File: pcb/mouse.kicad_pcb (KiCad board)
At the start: 2 copper layers, 70 x 45 mm, 74 parts, among them J1 USB_C_Receptacle_USB2.0, J2 Conn_01x05, J3 Conn_02x03_Counter_Clockwise, J4 Conn_01x06, J5 Conn_01x06, SW1 SW_Push_SPDT, SW2 SW_Push_SPDT, SW3 SW_Push_SPDT, SW4 SW_Push_SPDT, SW5 RotaryEncoder, SW6 SW_Push, U1 pmw3360-t2qu, U2 TLV70018_SOT23-5, U3 STM32F042K6Tx, U4 TLV70033_SOT23-5

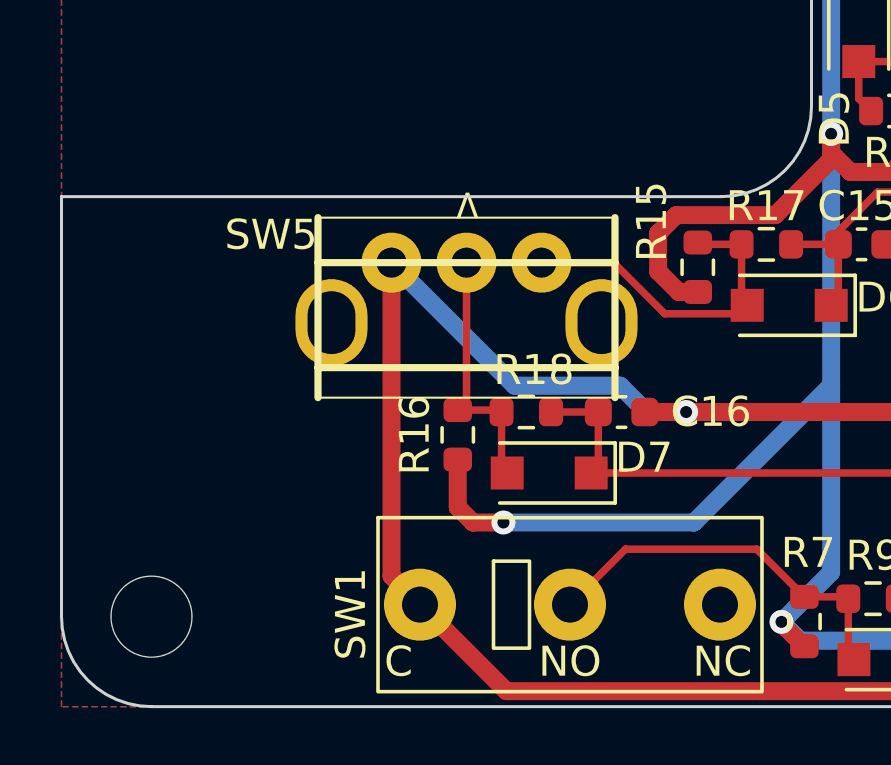
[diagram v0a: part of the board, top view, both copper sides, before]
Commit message: adjusted encoder position
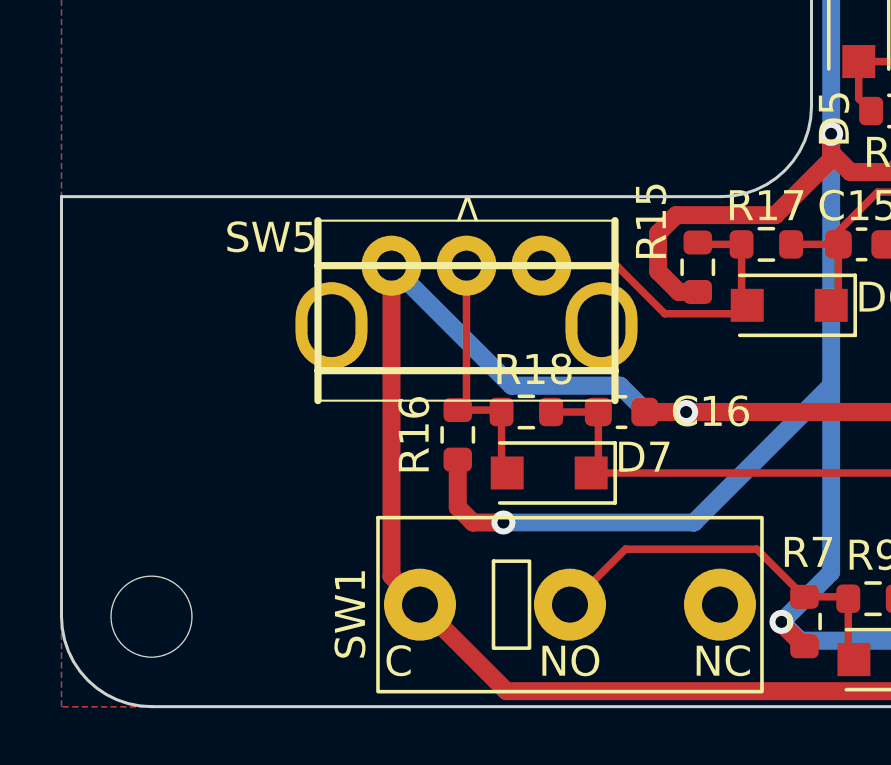
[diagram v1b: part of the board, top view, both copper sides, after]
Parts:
- moved SW5 0.10 mm to (113.5, 110.3)
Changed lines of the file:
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@@
   )
   (footprint "mouse:mouse_encoder" (layer "F.Cu")
-    (at 113.5 110.2 180)
+    (at 113.5 110.3 180)
     (property "Sheetfile" "buttons.kicad_sch")
     (property "Sheetname" "buttons")
@@
   (segment (start 111 120.65) (end 111.95 121.6) (width 0.6) (layer "F.Cu") (net 2))
   (segment (start 129.922 94.478) (end 130.82 94.478) (width 0.6) (layer "F.Cu") (net 2))
+  (segment (start 111 120.65) (end 111 110.3) (width 0.6) (layer "F.Cu") (net 2))
   (segment (start 107.005 93.915) (end 107.57 93.35) (width 0.6) (layer "F.Cu") (net 2))
   (segment (start 103.175 81.969) (end 103.769 81.969) (width 0.6) (layer "F.Cu") (net 2))
@@
   (segment (start 160.123 115.546) (end 161.10625 116.52925) (width 0.6) (layer "F.Cu") (net 2))
   (segment (start 140.214 95.113) (end 139.9186 95.113) (width 0.6) (layer "F.Cu") (net 2))
-  (segment (start 111 120.65) (end 111 110.2) (width 0.6) (layer "F.Cu") (net 2))
   (segment (start 129.8956 109.5502) (end 127.4858 109.5502) (width 0.6) (layer "F.Cu") (net 2))
   (via (at 123.571 91.821) (size 0.8) (drill 0.4) (layers "F.Cu" "B.Cu") (net 2))
@@
   (segment (start 138.14202 89.29782) (end 136.652 87.8078) (width 0.6) (layer "B.Cu") (net 2))
   (segment (start 123.571 91.821) (end 124.2568 91.821) (width 0.6) (layer "B.Cu") (net 2))
-  (segment (start 115.1 114.3) (end 111 110.2) (width 0.6) (layer "B.Cu") (net 2))
+  (segment (start 119.497 115.179) (end 118.618 114.3) (width 0.6) (layer "B.Cu") (net 2))
   (segment (start 110.0828 82.6) (end 110.8828 83.4) (width 0.6) (layer "B.Cu") (net 2))
   (segment (start 152.0124 86.5124) (end 147.7 82.2) (width 0.6) (layer "B.Cu") (net 2))
+  (segment (start 118.618 114.3) (end 115 114.3) (width 0.6) (layer "B.Cu") (net 2))
   (segment (start 138.14202 91.584193) (end 138.14202 89.29782) (width 0.6) (layer "B.Cu") (net 2))
   (segment (start 131.0984 115.452) (end 131.0984 119.77) (width 0.6) (layer "B.Cu") (net 2))
@@
   (segment (start 102.825 85.68) (end 102.825 94.32) (width 0.6) (layer "B.Cu") (net 2))
   (segment (start 102.825 85.68) (end 102.835034 85.690034) (width 0.6) (layer "B.Cu") (net 2))
+  (segment (start 115 114.3) (end 111 110.3) (width 0.6) (layer "B.Cu") (net 2))
   (segment (start 102.825 85.68) (end 102.9912 85.68) (width 0.6) (layer "B.Cu") (net 2))
-  (segment (start 119.497 115.179) (end 118.618 114.3) (width 0.6) (layer "B.Cu") (net 2))
   (segment (start 123.55 91.8) (end 112.15 91.8) (width 0.6) (layer "B.Cu") (net 2))
+  (segment (start 120.821 115.179) (end 119.497 115.179) (width 0.6) (layer "B.Cu") (net 2))
   (segment (start 152.7302 91.059) (end 152.2212 91.568) (width 0.6) (layer "B.Cu") (net 2))
   (segment (start 127.127 88.9508) (end 130.7084 88.9508) (width 0.6) (layer "B.Cu") (net 2))
@@
   (segment (start 155.2702 117.6528) (end 142.2654 117.6528) (width 0.6) (layer "B.Cu") (net 2))
   (segment (start 133.2992 117.6528) (end 142.2654 117.6528) (width 0.6) (layer "B.Cu") (net 2))
-  (segment (start 120.821 115.179) (end 119.497 115.179) (width 0.6) (layer "B.Cu") (net 2))
   (segment (start 140.4112 99.06) (end 140.3858 99.0346) (width 0.6) (layer "B.Cu") (net 2))
   (segment (start 154.7622 93.1926) (end 156.0796 93.1926) (width 0.6) (layer "B.Cu") (net 2))
@@
   (segment (start 104.4 82.6) (end 110.0828 82.6) (width 0.6) (layer "B.Cu") (net 2))
   (segment (start 124.2568 91.821) (end 127.127 88.9508) (width 0.6) (layer "B.Cu") (net 2))
-  (segment (start 118.618 114.3) (end 115.1 114.3) (width 0.6) (layer "B.Cu") (net 2))
   (segment (start 102.825 94.32) (end 107.005 94.32) (width 0.6) (layer "B.Cu") (net 2))
   (segment (start 132.7658 117.1194) (end 133.2992 117.6528) (width 0.6) (layer "B.Cu") (net 2))
@@
   (segment (start 122.67 111.436) (end 122.857 111.623) (width 0.25) (layer "F.Cu") (net 19))
   (segment (start 121.272 109.591) (end 121.209 109.528) (width 0.25) (layer "F.Cu") (net 19))
-  (segment (start 118.406676 110.2) (end 116 110.2) (width 0.25) (layer "F.Cu") (net 19))
+  (segment (start 120.109676 111.903) (end 118.506676 110.3) (width 0.25) (layer "F.Cu") (net 19))
+  (segment (start 118.506676 110.3) (end 116 110.3) (width 0.25) (layer "F.Cu") (net 19))
   (segment (start 122.67 109.591) (end 121.272 109.591) (width 0.25) (layer "F.Cu") (net 19))
-  (segment (start 120.109676 111.903) (end 118.406676 110.2) (width 0.25) (layer "F.Cu") (net 19))
   (segment (start 122.67 109.591) (end 122.67 111.436) (width 0.25) (layer "F.Cu") (net 19))
   (segment (start 122.857 111.623) (end 122.577 111.903) (width 0.25) (layer "F.Cu") (net 19))
+  (segment (start 113.208 115.116) (end 113.5 114.824) (width 0.25) (layer "F.Cu") (net 20))
   (segment (start 113.208 115.116) (end 114.606 115.116) (width 0.25) (layer "F.Cu") (net 20))
   (segment (start 114.669 117.024) (end 114.856 117.211) (width 0.25) (layer "F.Cu") (net 20))
-  (segment (start 113.208 115.116) (end 113.5 114.824) (width 0.25) (layer "F.Cu") (net 20))
+  (segment (start 113.5 114.824) (end 113.5 110.3) (width 0.25) (layer "F.Cu") (net 20))
   (segment (start 114.669 115.179) (end 114.669 117.024) (width 0.25) (layer "F.Cu") (net 20))
   (segment (start 114.606 115.116) (end 114.669 115.179) (width 0.25) (layer "F.Cu") (net 20))
-  (segment (start 113.5 114.824) (end 113.5 110.2) (width 0.25) (layer "F.Cu") (net 20))
   (segment (start 157.96875 118.364) (end 159.53125 118.364) (width 0.25) (layer "F.Cu") (net 21))
   (segment (start 157.96875 120.015) (end 159.53125 120.015) (width 0.25) (layer "F.Cu") (net 22))
